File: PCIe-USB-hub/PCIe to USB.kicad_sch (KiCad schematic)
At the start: 105 parts, among them Y1 X322524MQB4SI, Y2 X322524MQB4SI, Y3 X322524MQB4SI

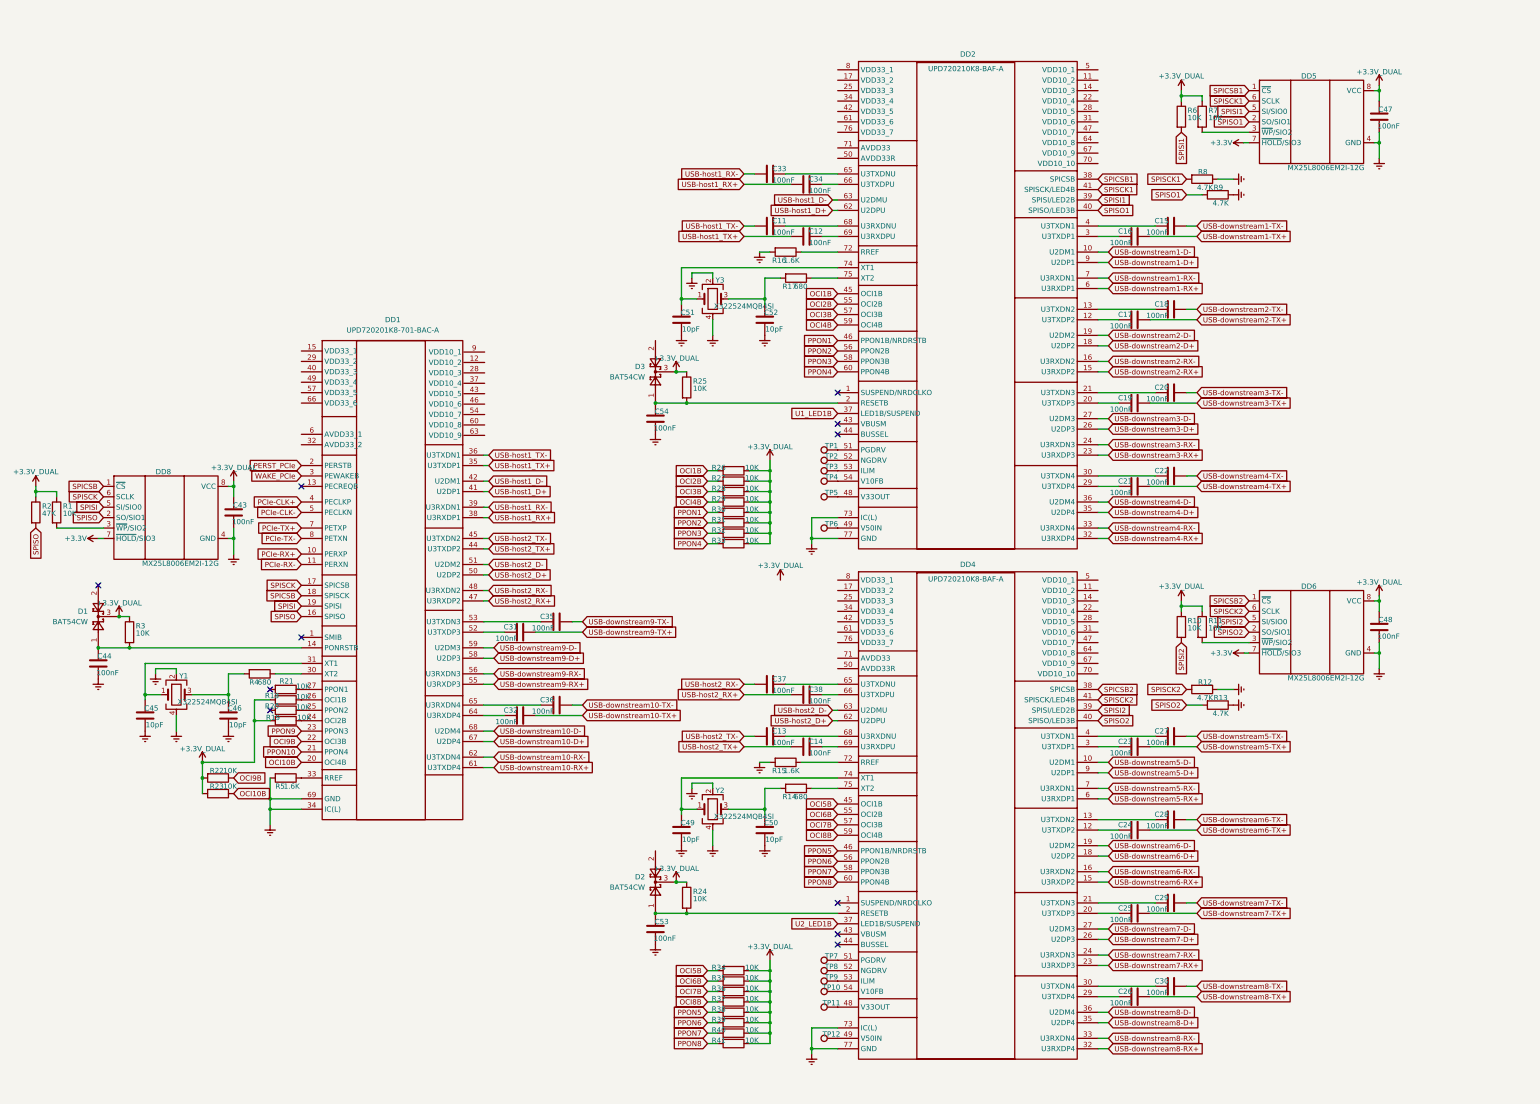
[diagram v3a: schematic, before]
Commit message: тык тык поменял разъёмы на одинарные
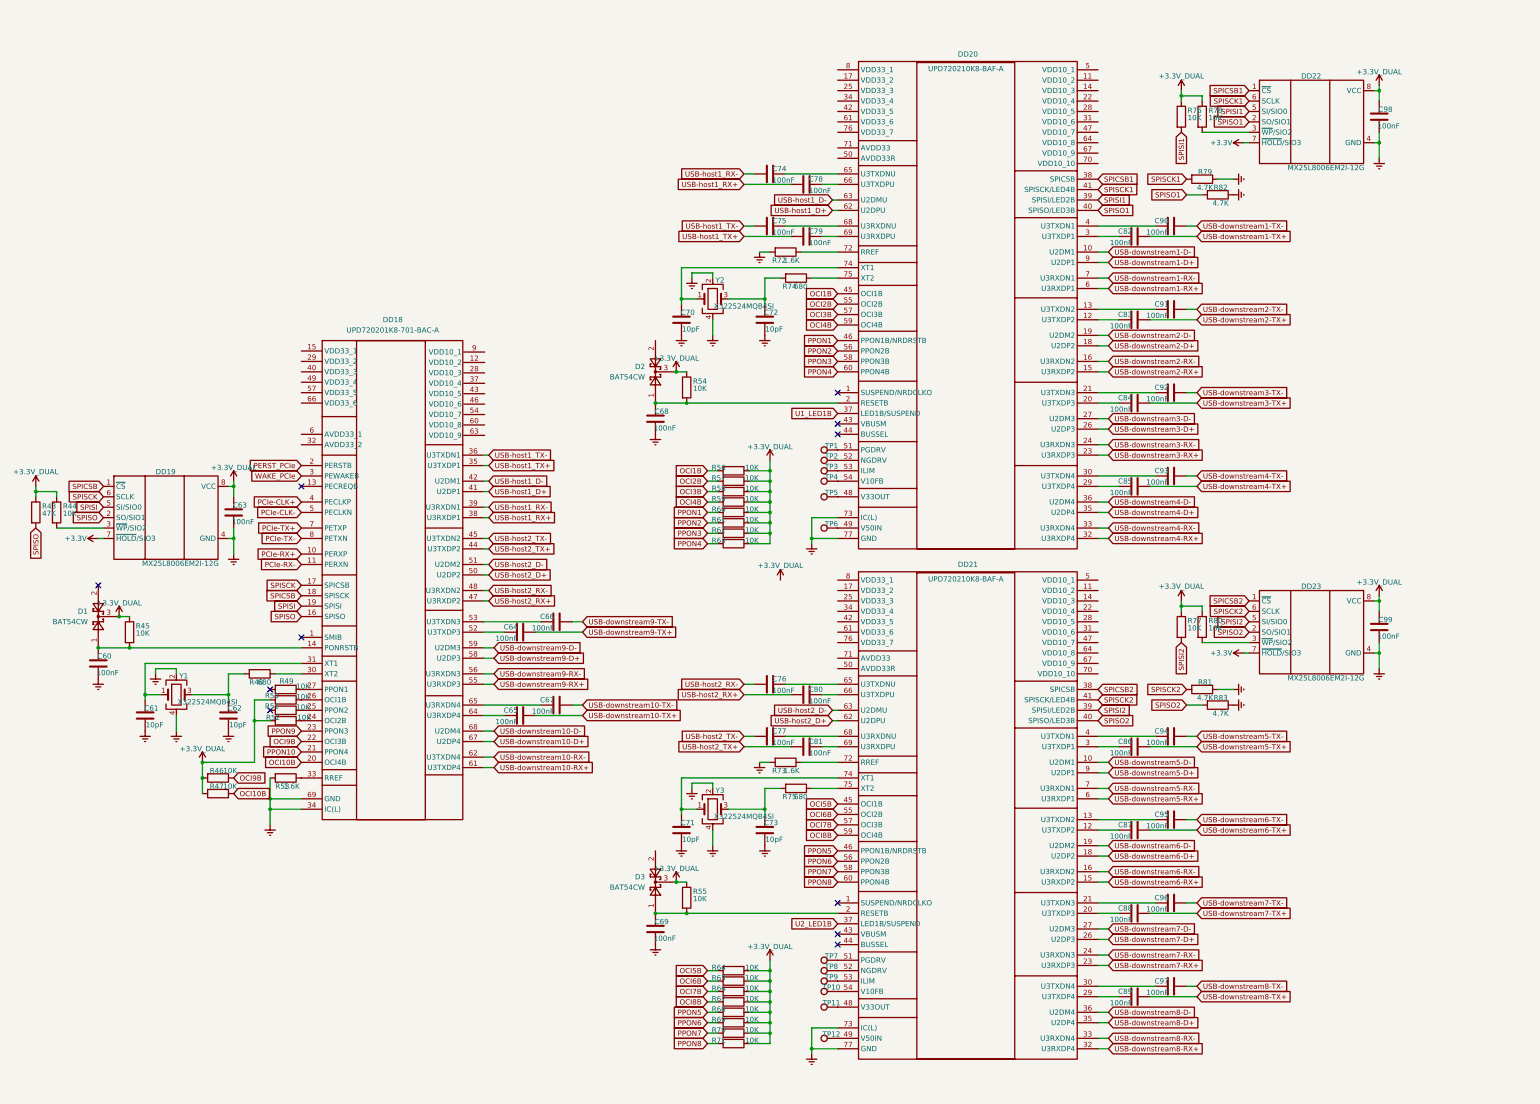
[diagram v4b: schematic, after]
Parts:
- renumbered C44 to C60, C45 to C61, C46 to C62, C43 to C63, C31 to C64, C32 to C65, C35 to C66, C36 to C67, C54 to C68, C53 to C69, C51 to C70, C49 to C71, C52 to C72, C50 to C73, C33 to C74, C11 to C75, C37 to C76, C13 to C77, C34 to C78, C12 to C79, C38 to C80, C14 to C81, C16 to C82, C17 to C83, C19 to C84, C21 to C85, C23 to C86, C24 to C87, C25 to C88, C26 to C89, C15 to C90, C18 to C91, C20 to C92, C22 to C93, C27 to C94, C28 to C95, C29 to C96, C30 to C97, C47 to C98, C48 to C99, D3 to D2, D2 to D3, DD1 to DD18, DD8 to DD19, DD2 to DD20, DD4 to DD21, DD5 to DD22, DD6 to DD23, R2 to R43, R1 to R44, R3 to R45, R22 to R46, R23 to R47, R4 to R48, R21 to R49, R18 to R50, R20 to R51, R19 to R52, R5 to R53, R25 to R54, R24 to R55, R26 to R56, R27 to R57, R28 to R58, R29 to R59, R30 to R60, R31 to R61, R32 to R62, R33 to R63, R34 to R64, R35 to R65, R36 to R66, R37 to R67, R38 to R68, R39 to R69, R40 to R70, R41 to R71, R16 to R72, R15 to R73, R17 to R74, R14 to R75, R6 to R76, R10 to R77, R7 to R78, R8 to R79, R11 to R80, R12 to R81, R9 to R82, R13 to R83, Y3 to Y2, Y2 to Y3

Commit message: натыкал трассировку всех дифф линий, поменял часть местами для удобной трассировки
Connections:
- net +3.3V is gone; now on net +3.3V_DUAL: DD19.7 (~{HOLD}/SIO3), DD22.7 (~{HOLD}/SIO3), DD23.7 (~{HOLD}/SIO3)
- net USB-downstream10-D+: now also DD18.58 (U2DP3); no longer DD18.67 (U2DP4)
- net USB-downstream10-D-: now also DD18.59 (U2DM3); no longer DD18.68 (U2DM4)
- net USB-downstream10-RX+: now also DD18.55 (U3RXDP3); no longer DD18.61 (U3TXDP4)
- net USB-downstream10-RX-: now also DD18.56 (U3RXDN3); no longer DD18.62 (U3TXDN4)
- net USB-downstream9-D+: now also DD18.67 (U2DP4); no longer DD18.58 (U2DP3)
- net USB-downstream9-D-: now also DD18.68 (U2DM4); no longer DD18.59 (U2DM3)
- net USB-downstream9-RX+: now also DD18.61 (U3TXDP4); no longer DD18.55 (U3RXDP3)
- net USB-downstream9-RX-: now also DD18.62 (U3TXDN4); no longer DD18.56 (U3RXDN3)
- net USB-host1_D+: now also DD18.50 (U2DP2); no longer DD18.41 (U2DP1)
- net USB-host1_D-: now also DD18.51 (U2DM2); no longer DD18.42 (U2DM1)
- net USB-host1_RX+: now also DD18.47 (U3RXDP2); no longer DD18.38 (U3RXDP1)
- net USB-host1_RX-: now also DD18.48 (U3RXDN2); no longer DD18.39 (U3RXDN1)
- net USB-host1_TX+: now also DD18.44 (U3TXDP2); no longer DD18.35 (U3TXDP1)
- net USB-host1_TX-: now also DD18.45 (U3TXDN2); no longer DD18.36 (U3TXDN1)
- net USB-host2_D+: now also DD18.41 (U2DP1); no longer DD18.50 (U2DP2)
- net USB-host2_D-: now also DD18.42 (U2DM1); no longer DD18.51 (U2DM2)
- net USB-host2_RX+: now also DD18.38 (U3RXDP1); no longer DD18.47 (U3RXDP2)
- net USB-host2_RX-: now also DD18.39 (U3RXDN1); no longer DD18.48 (U3RXDN2)
- net USB-host2_TX+: now also DD18.35 (U3TXDP1); no longer DD18.44 (U3TXDP2)
- net USB-host2_TX-: now also DD18.36 (U3TXDN1); no longer DD18.45 (U3TXDN2)
- net _USB-host2_TX-: now reaches C77.2, DD21.68 (U3RXDNU)
- net _USB-downstream1-TX+: now reaches C82.2, DD20.3 (U3TXDP1)
- net _USB-downstream10-TX-: now reaches DD18.53 (U3TXDN3)
- net _USB-downstream10-TX-: now also C67.2; no longer C66.2
- net _USB-downstream6-TX-: now reaches C95.2, DD21.13 (U3TXDN2)
- net _USB-downstream5-TX-: now reaches C94.2, DD21.4 (U3TXDN1)
- net _USB-downstream10-TX+: now reaches DD18.52 (U3TXDP3)
- net _USB-downstream10-TX+: now also C65.2; no longer C64.2
- net _USB-downstream5-TX+: now reaches C86.2, DD21.3 (U3TXDP1)
- net _USB-downstream1-TX-: now reaches C90.2, DD20.4 (U3TXDN1)
- net _USB-downstream9-TX+: now reaches DD18.64 (U3RXDP4)
- net _USB-downstream9-TX+: now also C64.2; no longer C65.2
- net _USB-downstream9-TX-: now reaches DD18.65 (U3RXDN4)
- net _USB-downstream9-TX-: now also C66.2; no longer C67.2
- net _USB-downstream7-TX-: now reaches C96.2, DD21.21 (U3TXDN3)
- net _USB-host2_RX-: now reaches C76.2, DD21.65 (U3TXDNU)
- net _USB-downstream2-TX+: now reaches C83.2, DD20.12 (U3TXDP2)
- net _USB-downstream2-TX-: now reaches C91.2, DD20.13 (U3TXDN2)
- net _USB-downstream3-TX+: now reaches C84.2, DD20.20 (U3TXDP3)
- net _USB-downstream3-TX-: now reaches C92.2, DD20.21 (U3TXDN3)
- net _USB-downstream4-TX+: now reaches C85.2, DD20.29 (U3TXDP4)
- net _USB-downstream4-TX-: now reaches C93.2, DD20.30 (U3TXDN4)
- net _USB-host1_RX-: now reaches C74.2, DD20.65 (U3TXDNU)
- net _USB-host1_RX+: now reaches C78.2, DD20.66 (U3TXDPU)
- net _USB-host1_TX-: now reaches C75.2, DD20.68 (U3RXDNU)
- net _USB-host1_TX+: now reaches C79.2, DD20.69 (U3RXDPU)
- net _USB-downstream8-TX-: now reaches C97.2, DD21.30 (U3TXDN4)
- net _USB-downstream6-TX+: now reaches C87.2, DD21.12 (U3TXDP2)
- net _USB-host2_TX+: now reaches C81.2, DD21.69 (U3RXDPU)
- net _USB-downstream7-TX+: now reaches C88.2, DD21.20 (U3TXDP3)
- net _USB-host2_RX+: now reaches C80.2, DD21.66 (U3TXDPU)
- net _USB-downstream8-TX+: now reaches C89.2, DD21.29 (U3TXDP4)
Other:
- moved on the sheet: C64, C65, C66, C67

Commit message: тык-перетык
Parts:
- added C100, C102, C104, C106, C108, C110, C112, C114, C116, C120, C121, C122, C126, C129, C130, C131, C135, C137, C138, C141, C142, C144, C145, C148, C149, C151, C153: 100nF, Capacitor_SMD:C_0402_1005Metric, symbol Device:C
- added C101, C103, C105, C107, C109, C111, C113, C115, C117, C118, C119, C123, C124, C125, C127, C128, C132, C133, C134, C136, C139, C140, C143, C146, C147, C150, C152: 22uF, Capacitor_SMD:C_0402_1005Metric, symbol Device:C
- added L10, L8, L9: 0.68uH, Inductor_SMD:L_Cenker_CKCS4020, symbol Device:L
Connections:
- net +3.3V_DUAL: now also DD18.15 (VDD33_1), DD18.29 (VDD33_2), DD18.40 (VDD33_3), DD18.49 (VDD33_4), DD18.57 (VDD33_5), DD18.66 (VDD33_6), DD20.17 (VDD33_2), DD20.25 (VDD33_3), DD20.34 (VDD33_4), DD20.42 (VDD33_5), DD20.61 (VDD33_6), DD20.76 (VDD33_7), DD20.8 (VDD33_1), DD21.17 (VDD33_2), DD21.25 (VDD33_3), DD21.34 (VDD33_4), DD21.42 (VDD33_5), DD21.61 (VDD33_6), DD21.76 (VDD33_7), DD21.8 (VDD33_1), C102.1, C103.1, C104.1, C105.1, C106.1, C107.1, C108.1, C136.1, C137.1, C138.1, C140.1, C142.1, C143.1, C144.1, C145.1, C146.1, C148.1, C150.1, C151.1, C152.1, C153.1, L10.1, L8.1, L9.1
- net Earth: now also C100.2, C101.2, C102.2, C103.2, C104.2, C105.2, C106.2, C107.2, C108.2, C109.2, C110.2, C111.2, C112.2, C113.2, C114.2, C115.2, C116.2, C117.2, C118.2, C119.2, C120.2, C121.2, C122.2, C123.2, C124.2, C125.2, C126.2, C127.2, C128.2, C129.2, C130.2, C131.2, C132.2, C133.2, C134.2, C135.2, C136.2, C137.2, C138.2, C139.2, C140.2, C141.2, C142.2, C143.2, C144.2, C145.2, C146.2, C147.2, C148.2, C149.2, C150.2, C151.2, C152.2, C153.2
- net 1.05V: now reaches DD18.12 (VDD10_2)
- net 1.05V: now also DD18.28 (VDD10_3), DD18.37 (VDD10_4), DD18.43 (VDD10_5), DD18.46 (VDD10_6), DD18.54 (VDD10_7), DD18.60 (VDD10_8), DD18.63 (VDD10_9), DD18.9 (VDD10_1), DD20.11 (VDD10_2), DD20.14 (VDD10_3), DD20.22 (VDD10_4), DD20.28 (VDD10_5), DD20.31 (VDD10_6), DD20.47 (VDD10_7), DD20.5 (VDD10_1), DD20.64 (VDD10_8), DD20.67 (VDD10_9), DD20.70 (VDD10_10), DD21.11 (VDD10_2), DD21.14 (VDD10_3), DD21.22 (VDD10_4), DD21.28 (VDD10_5), DD21.31 (VDD10_6), DD21.47 (VDD10_7), DD21.5 (VDD10_1), DD21.64 (VDD10_8), DD21.67 (VDD10_9), DD21.70 (VDD10_10), C109.1, C110.1, C111.1, C112.1, C113.1, C114.1, C115.1, C116.1, C117.1, C118.1, C119.1, C120.1, C121.1, C122.1, C123.1, C124.1, C125.1, C126.1, C127.1, C128.1, C129.1, C130.1, C131.1, C132.1, C133.1, C134.1, C135.1
- net at DD18.32 (AVDD33_2): now also DD18.6 (AVDD33_1), C100.1, C101.1, L8.2
- net at DD20.50 (AVDD33R): now also DD20.71 (AVDD33), C139.1, C141.1, L9.2
- net at DD21.50 (AVDD33R): now also DD21.71 (AVDD33), C147.1, C149.1, L10.2
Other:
- moved on the sheet: C63, C69, C71, C73, C76, C77, C80, C81, C86, C87, C88, C89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
